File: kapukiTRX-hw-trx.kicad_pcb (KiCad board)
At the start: 4 copper layers, 45.7 x 27.9 mm, 87 parts, among them J1 GPS, J10 Conn_01x01, J11 Conn_01x01, J12 Conn_01x01, J13 Conn_01x01, J14 Conn_01x01, J15 Conn_01x01, J16 Conn_01x01, J17 Conn_01x01, J18 Conn_01x01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

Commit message: Change some pins for better routing
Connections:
- U1 pad A4: /RF2MISO -> Net-(U1-PadA4)
- U1 pad B4: /RF2MOSI -> Net-(U1-PadB4)
- U1 pad B5: /RF2CLK -> Net-(U1-PadB5)
- U1 pad J1: Net-(U1-PadJ1) -> /RF2CLK
- U1 pad J2: Net-(U1-PadJ2) -> /RF2MISO
- U1 pad K1: Net-(U1-PadK1) -> /RF2MOSI
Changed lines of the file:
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@@
   (net 112 "Net-(U1-PadC3)")
   (net 113 "Net-(U1-PadB3)")
-  (net 114 "Net-(U1-PadJ2)")
-  (net 115 "Net-(U1-PadG2)")
-  (net 116 "Net-(U1-PadF2)")
-  (net 117 "Net-(U1-PadK1)")
-  (net 118 "Net-(U1-PadJ1)")
-  (net 119 "Net-(U1-PadF1)")
-  (net 120 "Net-(U1-PadD1)")
-  (net 121 "Net-(U1-PadC1)")
-  (net 122 /TXMODE)
-  (net 123 /SDA)
-  (net 124 /SCL)
-  (net 125 /BNORESET)
-  (net 126 /BNOINT)
-  (net 127 /BMPINT)
-  (net 128 /CANEN)
+  (net 114 "Net-(U1-PadG2)")
+  (net 115 "Net-(U1-PadF2)")
+  (net 116 "Net-(U1-PadF1)")
+  (net 117 "Net-(U1-PadD1)")
+  (net 118 "Net-(U1-PadC1)")
+  (net 119 /TXMODE)
+  (net 120 /SDA)
+  (net 121 /SCL)
+  (net 122 /BNORESET)
+  (net 123 /BNOINT)
+  (net 124 /BMPINT)
+  (net 125 /CANEN)
+  (net 126 "Net-(U1-PadB5)")
+  (net 127 "Net-(U1-PadB4)")
+  (net 128 "Net-(U1-PadA4)")
   (net_class Default "This is the default net class."
     (clearance 0.127)
@@
     (add_net "Net-(R5-Pad1)")
     (add_net "Net-(R8-Pad1)")
+    (add_net "Net-(U1-PadA4)")
     (add_net "Net-(U1-PadA9)")
     (add_net "Net-(U1-PadB3)")
+    (add_net "Net-(U1-PadB4)")
+    (add_net "Net-(U1-PadB5)")
     (add_net "Net-(U1-PadB7)")
     (add_net "Net-(U1-PadB8)")
@@
     (add_net "Net-(U1-PadH5)")
     (add_net "Net-(U1-PadH6)")
-    (add_net "Net-(U1-PadJ1)")
-    (add_net "Net-(U1-PadJ2)")
     (add_net "Net-(U1-PadJ4)")
     (add_net "Net-(U1-PadJ6)")
     (add_net "Net-(U1-PadJ7)")
     (add_net "Net-(U1-PadJ8)")
-    (add_net "Net-(U1-PadK1)")
     (add_net "Net-(U1-PadK5)")
     (add_net "Net-(U7-Pad1)")
@@
       (net 88 "Net-(U1-PadJ8)"))
     (pad H8 smd circle (at 2 2) (size 0.36 0.36) (layers F.Cu F.Paste F.Mask)
-      (net 126 /BNOINT))
+      (net 123 /BNOINT))
     (pad G8 smd circle (at 2 1.2) (size 0.36 0.36) (layers F.Cu F.Paste F.Mask)
-      (net 127 /BMPINT))
+      (net 124 /BMPINT))
     (pad F8 smd circle (at 2 0.4) (size 0.36 0.36) (layers F.Cu F.Paste F.Mask)
       (net 89 "Net-(U1-PadF8)"))
@@
       (net 93 "Net-(U1-PadJ7)"))
     (pad H7 smd circle (at 1.2 2) (size 0.36 0.36) (layers F.Cu F.Paste F.Mask)
-      (net 125 /BNORESET))
+      (net 122 /BNORESET))
     (pad G7 smd circle (at 1.2 1.2) (size 0.36 0.36) (layers F.Cu F.Paste F.Mask)
       (net 94 "Net-(U1-PadG7)"))
@@
       (net 96 "Net-(U1-PadB7)"))
     (pad A7 smd circle (at 1.2 -3.6) (size 0.36 0.36) (layers F.Cu F.Paste F.Mask)
-      (net 122 /TXMODE))
+      (net 119 /TXMODE))
     (pad K6 smd circle (at 0.4 3.6) (size 0.36 0.36) (layers F.Cu F.Paste F.Mask)
       (net 22 /RF2IRQ))
@@
       (net 52 /CANTX))
     (pad B5 smd circle (at -0.4 -2.8) (size 0.36 0.36) (layers F.Cu F.Paste F.Mask)
-      (net 16 /RF2CLK))
+      (net 126 "Net-(U1-PadB5)"))
     (pad A5 smd circle (at -0.4 -3.6) (size 0.36 0.36) (layers F.Cu F.Paste F.Mask)
       (net 38 /GPSRX))
@@
       (net 108 "Net-(U1-PadC4)"))
     (pad B4 smd circle (at -1.2 -2.8) (size 0.36 0.36) (layers F.Cu F.Paste F.Mask)
-      (net 15 /RF2MOSI))
+      (net 127 "Net-(U1-PadB4)"))
     (pad A4 smd circle (at -1.2 -3.6) (size 0.36 0.36) (layers F.Cu F.Paste F.Mask)
-      (net 14 /RF2MISO))
+      (net 128 "Net-(U1-PadA4)"))
     (pad K3 smd circle (at -2 3.6) (size 0.36 0.36) (layers F.Cu F.Paste F.Mask)
       (net 19 /RF2TXEN))
@@
       (net 113 "Net-(U1-PadB3)"))
     (pad A3 smd circle (at -2 -3.6) (size 0.36 0.36) (layers F.Cu F.Paste F.Mask)
-      (net 124 /SCL))
+      (net 121 /SCL))
     (pad K2 smd circle (at -2.8 3.6) (size 0.36 0.36) (layers F.Cu F.Paste F.Mask)
       (net 21 /RF2BUSY))
     (pad J2 smd circle (at -2.8 2.8) (size 0.36 0.36) (layers F.Cu F.Paste F.Mask)
-      (net 114 "Net-(U1-PadJ2)"))
+      (net 14 /RF2MISO))
     (pad H2 smd circle (at -2.8 2) (size 0.36 0.36) (layers F.Cu F.Paste F.Mask)
       (net 17 /RF2NSS))
     (pad G2 smd circle (at -2.8 1.2) (size 0.36 0.36) (layers F.Cu F.Paste F.Mask)
-      (net 115 "Net-(U1-PadG2)"))
+      (net 114 "Net-(U1-PadG2)"))
     (pad F2 smd circle (at -2.8 0.4) (size 0.36 0.36) (layers F.Cu F.Paste F.Mask)
-      (net 116 "Net-(U1-PadF2)"))
+      (net 115 "Net-(U1-PadF2)"))
     (pad E2 smd circle (at -2.8 -0.4) (size 0.36 0.36) (layers F.Cu F.Paste F.Mask)
       (net 57 "Net-(C4-Pad1)"))
@@
       (net 1 GND))
     (pad C2 smd circle (at -2.8 -2) (size 0.36 0.36) (layers F.Cu F.Paste F.Mask)
-      (net 128 /CANEN))
+      (net 125 /CANEN))
     (pad B2 smd circle (at -2.8 -2.8) (size 0.36 0.36) (layers F.Cu F.Paste F.Mask)
       (net 41 /LEDRED))
     (pad A2 smd circle (at -2.8 -3.6) (size 0.36 0.36) (layers F.Cu F.Paste F.Mask)
-      (net 123 /SDA))
+      (net 120 /SDA))
     (pad K1 smd circle (at -3.6 3.6) (size 0.36 0.36) (layers F.Cu F.Paste F.Mask)
-      (net 117 "Net-(U1-PadK1)"))
+      (net 15 /RF2MOSI))
     (pad J1 smd circle (at -3.6 2.8) (size 0.36 0.36) (layers F.Cu F.Paste F.Mask)
-      (net 118 "Net-(U1-PadJ1)"))
+      (net 16 /RF2CLK))
     (pad H1 smd circle (at -3.6 2) (size 0.36 0.36) (layers F.Cu F.Paste F.Mask)
       (net 47 /PWM6))
@@
       (net 18 /RF2RXEN))
     (pad F1 smd circle (at -3.6 0.4) (size 0.36 0.36) (layers F.Cu F.Paste F.Mask)
-      (net 119 "Net-(U1-PadF1)"))
+      (net 116 "Net-(U1-PadF1)"))
     (pad E1 smd circle (at -3.6 -0.4) (size 0.36 0.36) (layers F.Cu F.Paste F.Mask)
       (net 56 "Net-(C3-Pad1)"))
     (pad D1 smd circle (at -3.6 -1.2) (size 0.36 0.36) (layers F.Cu F.Paste F.Mask)
-      (net 120 "Net-(U1-PadD1)"))
+      (net 117 "Net-(U1-PadD1)"))
     (pad C1 smd circle (at -3.6 -2) (size 0.36 0.36) (layers F.Cu F.Paste F.Mask)
-      (net 121 "Net-(U1-PadC1)"))
+      (net 118 "Net-(U1-PadC1)"))
     (pad B1 smd circle (at -3.6 -2.8) (size 0.36 0.36) (layers F.Cu F.Paste F.Mask)
       (net 43 /LEDBLUE))
@@
       (net 1 GND))
     (pad 14 smd rect (at 1.75 1.6625 90) (size 0.254 0.675) (layers F.Cu F.Paste F.Mask)
-      (net 126 /BNOINT))
+      (net 123 /BNOINT))
     (pad 13 smd rect (at 1.25 1.6625 90) (size 0.254 0.675) (layers F.Cu F.Paste F.Mask)
       (net 73 "Net-(U7-Pad13)"))
@@
       (net 74 "Net-(U7-Pad12)"))
     (pad 11 smd rect (at 0.25 1.6625 90) (size 0.254 0.675) (layers F.Cu F.Paste F.Mask)
-      (net 125 /BNORESET))
+      (net 122 /BNORESET))
     (pad 10 smd rect (at -0.25 1.6625 90) (size 0.254 0.675) (layers F.Cu F.Paste F.Mask)
       (net 75 "Net-(U7-Pad10)"))
@@
       (net 77 "Net-(U7-Pad7)"))
     (pad 20 smd rect (at 2.25 -1.6625 90) (size 0.254 0.675) (layers F.Cu F.Paste F.Mask)
-      (net 123 /SDA))
+      (net 120 /SDA))
     (pad 21 smd rect (at 1.75 -1.6625 90) (size 0.254 0.675) (layers F.Cu F.Paste F.Mask)
       (net 78 "Net-(U7-Pad21)"))
@@
       (net 1 GND))
     (pad 19 smd rect (at 2.3875 -0.75 180) (size 0.254 0.675) (layers F.Cu F.Paste F.Mask)
-      (net 124 /SCL))
+      (net 121 /SCL))
     (model ${KISYS3DMOD}/Package_LGA.3dshapes/LGA-28_5.2x3.8mm_P0.5mm.wrl
       (at (xyz 0 0 0))
@@
     (fp_line (start -0.5 0.25) (end -0.5 -0.25) (layer F.Fab) (width 0.1))
     (pad 2 smd roundrect (at 0.485 0 270) (size 0.59 0.64) (layers F.Cu F.Paste F.Mask) (roundrect_rratio 0.25)
-      (net 125 /BNORESET))
+      (net 122 /BNORESET))
     (pad 1 smd roundrect (at -0.485 0 270) (size 0.59 0.64) (layers F.Cu F.Paste F.Mask) (roundrect_rratio 0.25)
       (net 25 /VCCCPU))
@@
     (fp_line (start -0.5 0.25) (end -0.5 -0.25) (layer F.Fab) (width 0.1))
     (pad 2 smd roundrect (at 0.485 0 270) (size 0.59 0.64) (layers F.Cu F.Paste F.Mask) (roundrect_rratio 0.25)
-      (net 124 /SCL))
+      (net 121 /SCL))
     (pad 1 smd roundrect (at -0.485 0 270) (size 0.59 0.64) (layers F.Cu F.Paste F.Mask) (roundrect_rratio 0.25)
       (net 25 /VCCCPU))
@@
     (fp_line (start -0.5 0.25) (end -0.5 -0.25) (layer F.Fab) (width 0.1))
     (pad 2 smd roundrect (at 0.485 0 270) (size 0.59 0.64) (layers F.Cu F.Paste F.Mask) (roundrect_rratio 0.25)
-      (net 123 /SDA))
+      (net 120 /SDA))
     (pad 1 smd roundrect (at -0.485 0 270) (size 0.59 0.64) (layers F.Cu F.Paste F.Mask) (roundrect_rratio 0.25)
       (net 25 /VCCCPU))
@@
     )
     (pad 1 smd roundrect (at -0.485 0) (size 0.59 0.64) (layers F.Cu F.Paste F.Mask) (roundrect_rratio 0.25)
-      (net 122 /TXMODE))
+      (net 119 /TXMODE))
     (pad 2 smd roundrect (at 0.485 0) (size 0.59 0.64) (layers F.Cu F.Paste F.Mask) (roundrect_rratio 0.25)
       (net 1 GND))
@@
       (net 67 "Net-(J20-Pad1)"))
     (pad 8 smd rect (at 1.55 -0.975 180) (size 0.65 0.35) (layers F.Cu F.Paste F.Mask)
-      (net 128 /CANEN))
+      (net 125 /CANEN))
     (pad "" smd rect (at -0.3875 0.6 180) (size 0.6 1) (layers F.Paste))
     (pad 9 smd rect (at 0 0 180) (size 1.55 2.4) (layers F.Cu F.Mask)
@@
   (segment (start 195.707 111.633) (end 194.964901 110.890901) (width 0.127) (layer F.Cu) (net 72))
   (segment (start 194.564 110.694622) (end 194.564 110.363) (width 0.127) (layer F.Cu) (net 72))
-  (segment (start 196.437 107.7) (end 196.814 108.077) (width 0.127) (layer F.Cu) (net 125))
-  (segment (start 195.9725 107.7) (end 196.437 107.7) (width 0.127) (layer F.Cu) (net 125))
-  (segment (start 196.814 108.077) (end 197.358 108.077) (width 0.127) (layer F.Cu) (net 125))
+  (segment (start 196.437 107.7) (end 196.814 108.077) (width 0.127) (layer F.Cu) (net 122))
+  (segment (start 195.9725 107.7) (end 196.437 107.7) (width 0.127) (layer F.Cu) (net 122))
+  (segment (start 196.814 108.077) (end 197.358 108.077) (width 0.127) (layer F.Cu) (net 122))
   (zone (net 1) (net_name GND) (layer In1.Cu) (hatch edge 0.508)
     (connect_pads yes (clearance 0.254))

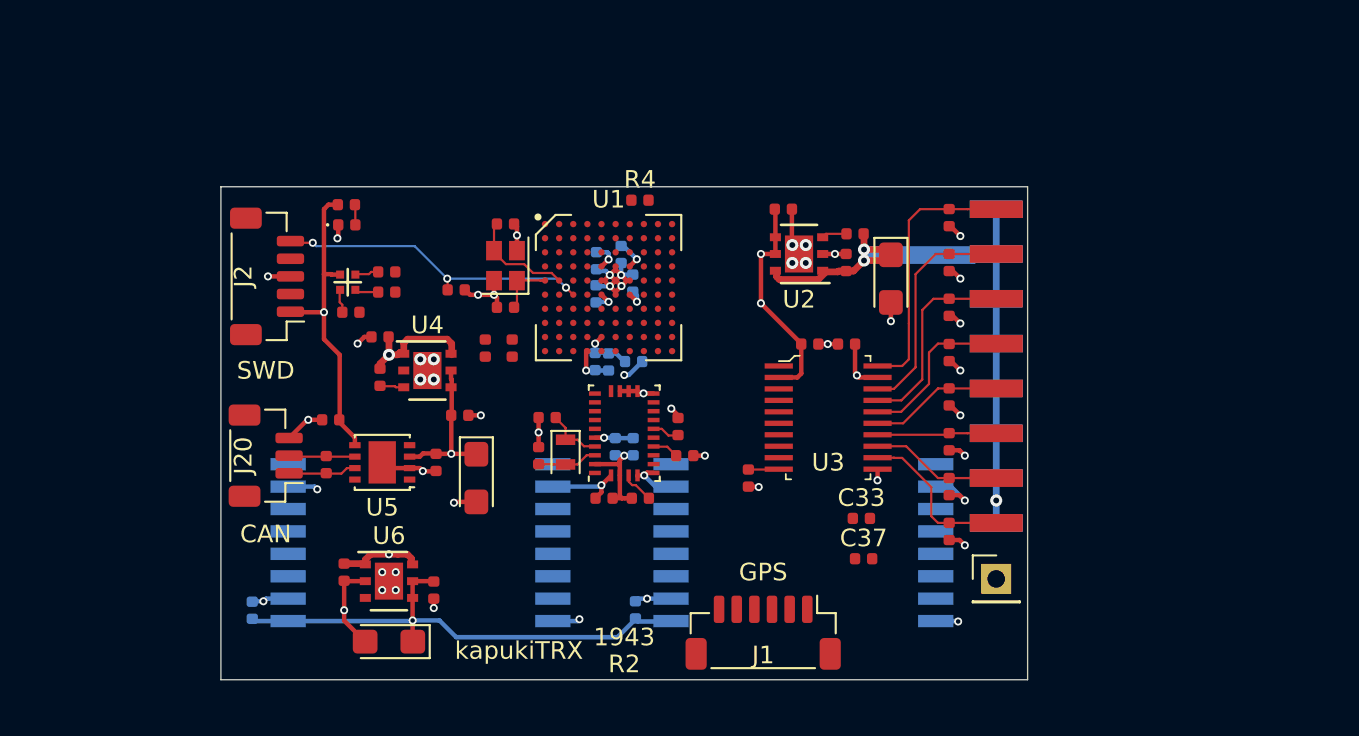
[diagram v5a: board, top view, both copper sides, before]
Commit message: Add proper footprint for BMP388
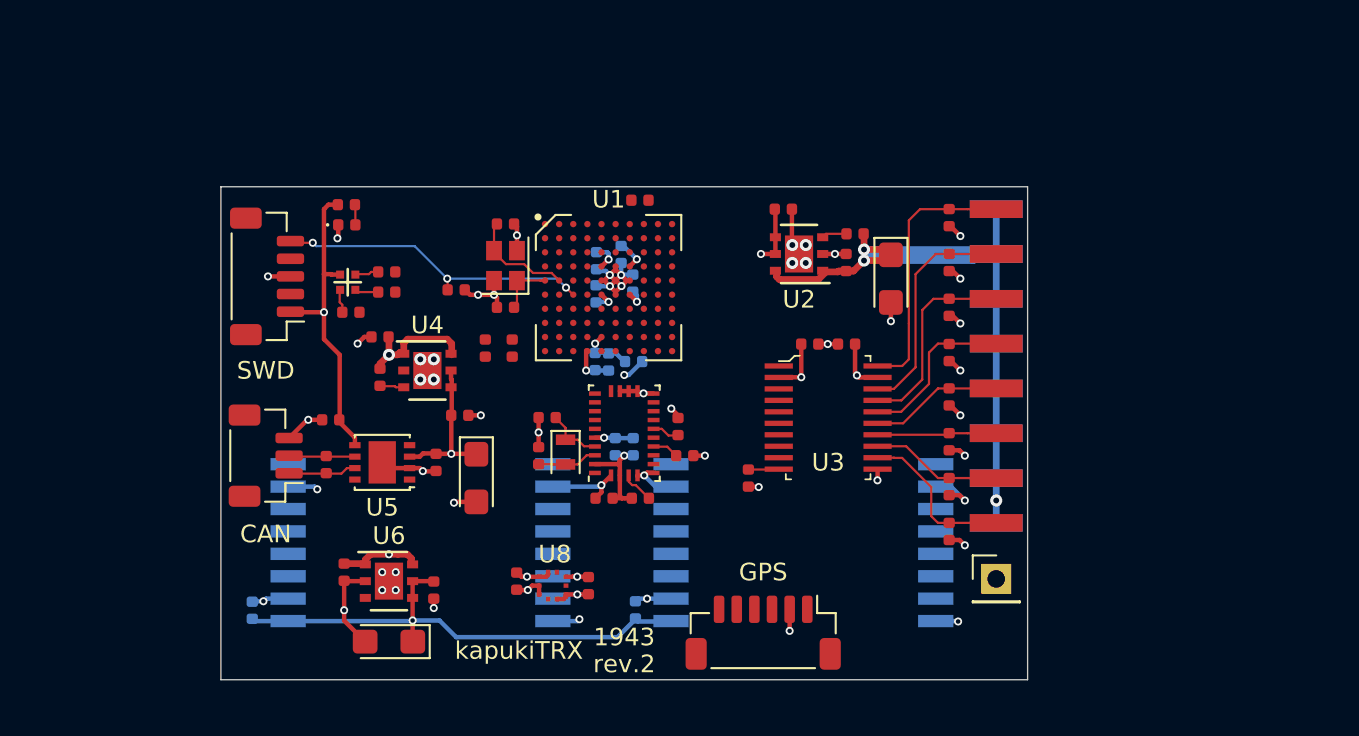
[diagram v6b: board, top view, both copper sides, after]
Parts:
- added U8: BMP388, miscellaneous:Bosch_LGA10_2x2mm_Pitch0.5mm, F.Cu at (190.2, 116.6)
- moved C33 19.9 mm to (188.2, 116.3), turned to 270 degrees
- moved C37 15.7 mm to (192.3, 116.6), turned to 270 degrees
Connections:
- U1 pad A1: /LEDGREEN -> /LEDBLUE
- U1 pad B1: /LEDBLUE -> /LEDGREEN
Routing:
- net /VCCCPU: track 92.1 -> 42.6 mm, vias 10 -> 12
- net GND: track 71.9 -> 76.3 mm, vias 53 -> 56
- added copper zone on In2.Cu, net /VCCCPU
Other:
- board text added: "G"
- board text added: "P"
- board text added: "rev.2"
- board text removed: "R2"

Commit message: Small changes
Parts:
- moved R4 2.41 mm to (192.8, 94.7)
- moved C37 2.32 mm to (190.7, 118.3), turned to 180 degrees
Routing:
- net /GPSTX: track 0.00 -> 22.8 mm
- net /GPSEN: track 0.00 -> 21.0 mm
- net /GPSPPS: track 0.00 -> 20.8 mm
- net /GPSRX: track 0.00 -> 19.8 mm, vias 0 -> 1
- net /SDA: track 0.00 -> 18.7 mm, vias 0 -> 2
- net /SCL: track 0.00 -> 16.8 mm, vias 0 -> 2
- net /LEDGREEN: track 0.00 -> 13.4 mm
- net /LEDRED: track 0.00 -> 12.0 mm
- net /LEDBLUE: track 0.00 -> 10.8 mm
- net /PWM4: track 0.00 -> 4.85 mm
- net /PWM3: track 0.00 -> 4.45 mm
- net /VCCCPU: track 42.6 -> 45.9 mm, vias 12 -> 14
- net /PWM2: track 0.00 -> 2.49 mm
- net GND: track 76.3 -> 77.9 mm
- net /PWM1: track 0.00 -> 1.55 mm
